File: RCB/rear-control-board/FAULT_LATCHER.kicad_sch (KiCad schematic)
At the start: 8 parts, among them J4 Conn_01x02, J5 Conn_01x02, K2 G5V-2, K3 G5V-2, Q1 BSS84, Q2 2N7002

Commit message: working on layout
Updating traces for RCB and organizing HVB
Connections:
- net bms_switch: now reaches D4.2 (A), J4.1 (Pin_1), K2.1, K2.8, Q1.1 (G)
- net connector: now reaches K2.13, K3.9
- net imd_switch: now reaches D5.1 (K), J5.2 (Pin_2), K3.1, K3.8, Q2.1 (G)
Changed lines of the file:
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@@
+    (effects (font (size 1.27 1.27)) (justify left bottom))
+  )
+  (label "bms_switch" (at 85.09 67.31 90)
     (effects (font (size 1.27 1.27)) (justify left bottom))
   )
@@
     (effects (font (size 1.27 1.27)) (justify right bottom))
   )
+  (label "connector" (at 118.11 46.99 180)
+    (effects (font (size 1.27 1.27)) (justify right bottom))
+  )
+  (label "imd_switch" (at 135.255 67.31 270)
+    (effects (font (size 1.27 1.27)) (justify right bottom))
+  )

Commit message: trace layout complete (need review)
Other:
- note added: "BMS BMS_FAULT_SIG is LOW Clear, HIGH Fault BMS_IND is HIGH when clear, pulled low when fault"
- note added: "IMD IMD_FAULT_SIG is HIGH Clear, LOW Fault IMD_IND is LOW when clear, pulled HIGH when fault"
- note removed: "BMS LOW Clear, HIGH Fault BMS_IND is HIGH when clear, pulled low when fault"
- note removed: "IMD HIGH Clear, LOW Fault IMD_IND is LOW when clear, pulled HIGH when fault"
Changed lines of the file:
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@@
     (effects (font (size 1.27 1.27)) (justify right bottom))
   )
-  (text "IMD\nHIGH Clear, LOW Fault\nIMD_IND is LOW when clear, \npulled HIGH when fault"
+  (text "IMD\nIMD_FAULT_SIG is HIGH Clear, LOW Fault\nIMD_IND is LOW when clear, \npulled HIGH when fault"
     (at 136.525 33.655 0)
     (effects (font (size 1.27 1.27)) (justify left bottom))
   )
-  (text "BMS\nLOW Clear, HIGH Fault\nBMS_IND is HIGH when clear, \npulled low when fault"
+  (text "BMS\nBMS_FAULT_SIG is LOW Clear, HIGH Fault\nBMS_IND is HIGH when clear, \npulled low when fault"
     (at 85.725 33.655 0)
     (effects (font (size 1.27 1.27)) (justify left bottom))

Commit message: Major Review and Part Update
updating footprints, component values, layouts
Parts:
- D4, D5: footprint Diode_THT:D_DO-35_SOD27_P7.62mm_Horizontal -> Diode_SMD:D_SOD-123
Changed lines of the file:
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@@
     (property "Reference" "D5" (id 0) (at 144.78 78.9432 0))
     (property "Value" "1N4148" (id 1) (at 144.78 81.2546 0))
-    (property "Footprint" "Diode_THT:D_DO-35_SOD27_P7.62mm_Horizontal" (id 2) (at 144.78 88.9 0)
+    (property "Footprint" "Diode_SMD:D_SOD-123" (id 2) (at 144.78 88.9 0)
       (effects (font (size 1.27 1.27)) hide)
     )
@@
     (property "Reference" "D4" (id 0) (at 96.52 74.4982 0))
     (property "Value" "1N4148" (id 1) (at 96.52 76.8096 0))
-    (property "Footprint" "Diode_THT:D_DO-35_SOD27_P7.62mm_Horizontal" (id 2) (at 96.52 75.565 0)
+    (property "Footprint" "Diode_SMD:D_SOD-123" (id 2) (at 96.52 75.565 0)
       (effects (font (size 1.27 1.27)) hide)
     )

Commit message: willem review notes
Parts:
- J4, J5: value Conn_01x02 -> JST-B2B-VERT-2PIN
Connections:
- net connector: no longer names the net of K2.13, K3.9
- no-connect marks 0 -> 4
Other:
- note added: "Instead of transistors, use voltage divider and zener diodes"
- note added: "UPERCASE LOCAL NETS ALSO SPREAD OUT SCHEM"
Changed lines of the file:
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@@
   (junction (at 106.68 67.31) (diameter 0) (color 0 0 0 0)
   )
+  (no_connect (at 88.9 49.53))
+  (no_connect (at 88.9 59.69))
+  (no_connect (at 137.16 59.69))
+  (no_connect (at 137.16 49.53))
   (wire (pts (xy 155.575 84.455) (xy 155.575 67.31))
     (stroke (width 0) (type default) (color 0 0 0 0))
@@
     (effects (font (size 1.27 1.27)) (justify right bottom))
   )
+  (text "UPERCASE LOCAL NETS\n\nALSO SPREAD OUT SCHEM" (at 177.165 78.105 0)
+    (effects (font (size 1.27 1.27)) (justify left bottom))
+  )
   (text "IMD\nIMD_FAULT_SIG is HIGH Clear, LOW Fault\nIMD_IND is LOW when clear, \npulled HIGH when fault"
     (at 136.525 33.655 0)
     (effects (font (size 1.27 1.27)) (justify left bottom))
   )
+  (text "Instead of transistors, use voltage divider\nand zener diodes"
+    (at 115.57 107.95 0)
+    (effects (font (size 1.27 1.27)) (justify left bottom))
+  )
   (text "BMS\nBMS_FAULT_SIG is LOW Clear, HIGH Fault\nBMS_IND is HIGH when clear, \npulled low when fault"
     (at 85.725 33.655 0)
@@
   (label "bms_switch" (at 85.09 67.31 90)
     (effects (font (size 1.27 1.27)) (justify left bottom))
-  )
-  (label "Loop_IN" (at 80.645 44.45 0)
-    (effects (font (size 1.27 1.27)) (justify left bottom))
-  )
-  (label "Loop_Out" (at 161.925 46.99 180)
-    (effects (font (size 1.27 1.27)) (justify right bottom))
-  )
-  (label "connector" (at 118.11 46.99 180)
-    (effects (font (size 1.27 1.27)) (justify right bottom))
   )
   (label "imd_switch" (at 135.255 67.31 270)
@@
       (effects (font (size 1.27 1.27)) (justify right))
     )
-    (property "Value" "Conn_01x02" (id 1) (at 120.65 59.69 90)
+    (property "Value" "JST-B2B-VERT-2PIN" (id 1) (at 114.935 59.69 90)
       (effects (font (size 1.27 1.27)) (justify right))
     )
@@
       (effects (font (size 1.27 1.27)) (justify right))
     )
-    (property "Value" "Conn_01x02" (id 1) (at 92.71 85.725 90)
-      (effects (font (size 1.27 1.27)) (justify right))
-    )
+    (property "Value" "JST-B2B-VERT-2PIN" (id 1) (at 92.71 85.725 90)
+      (effects (font (size 1.27 1.27)) (justify right))
+    )

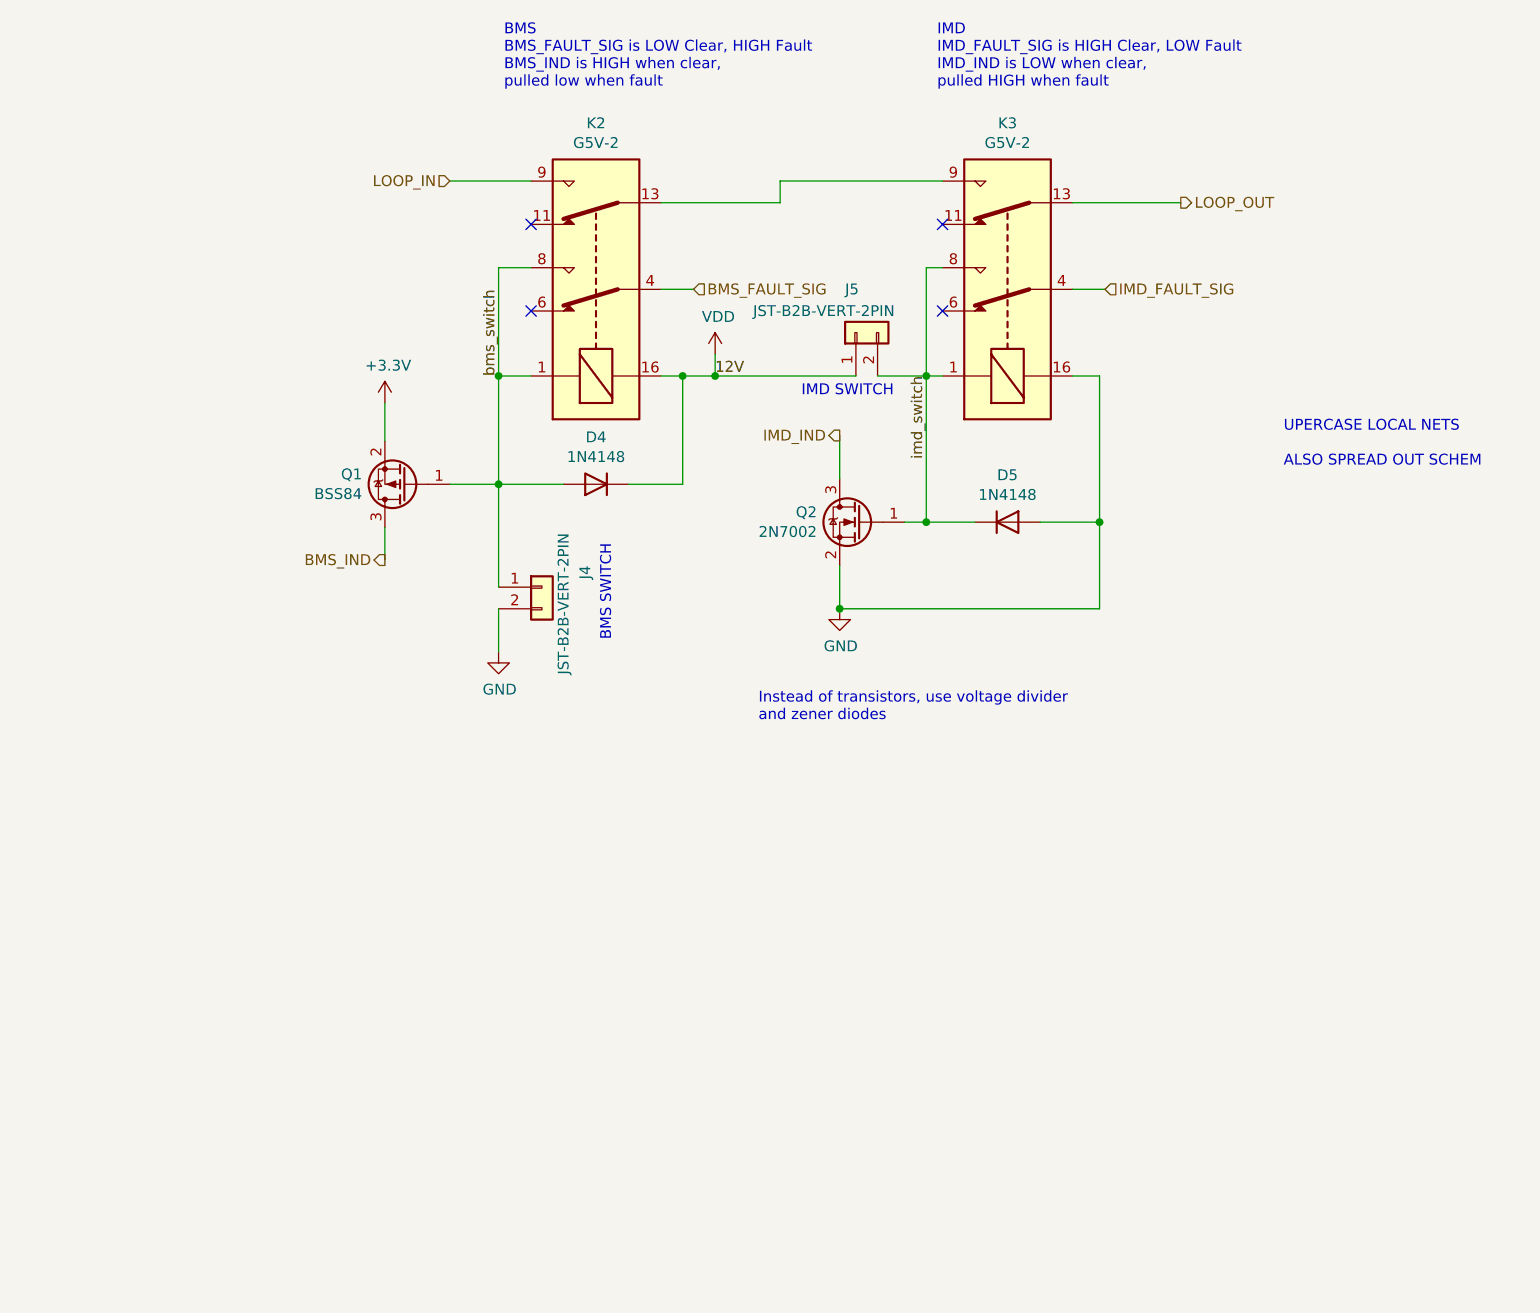
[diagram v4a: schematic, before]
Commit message: updating schem with design notes (major changes)
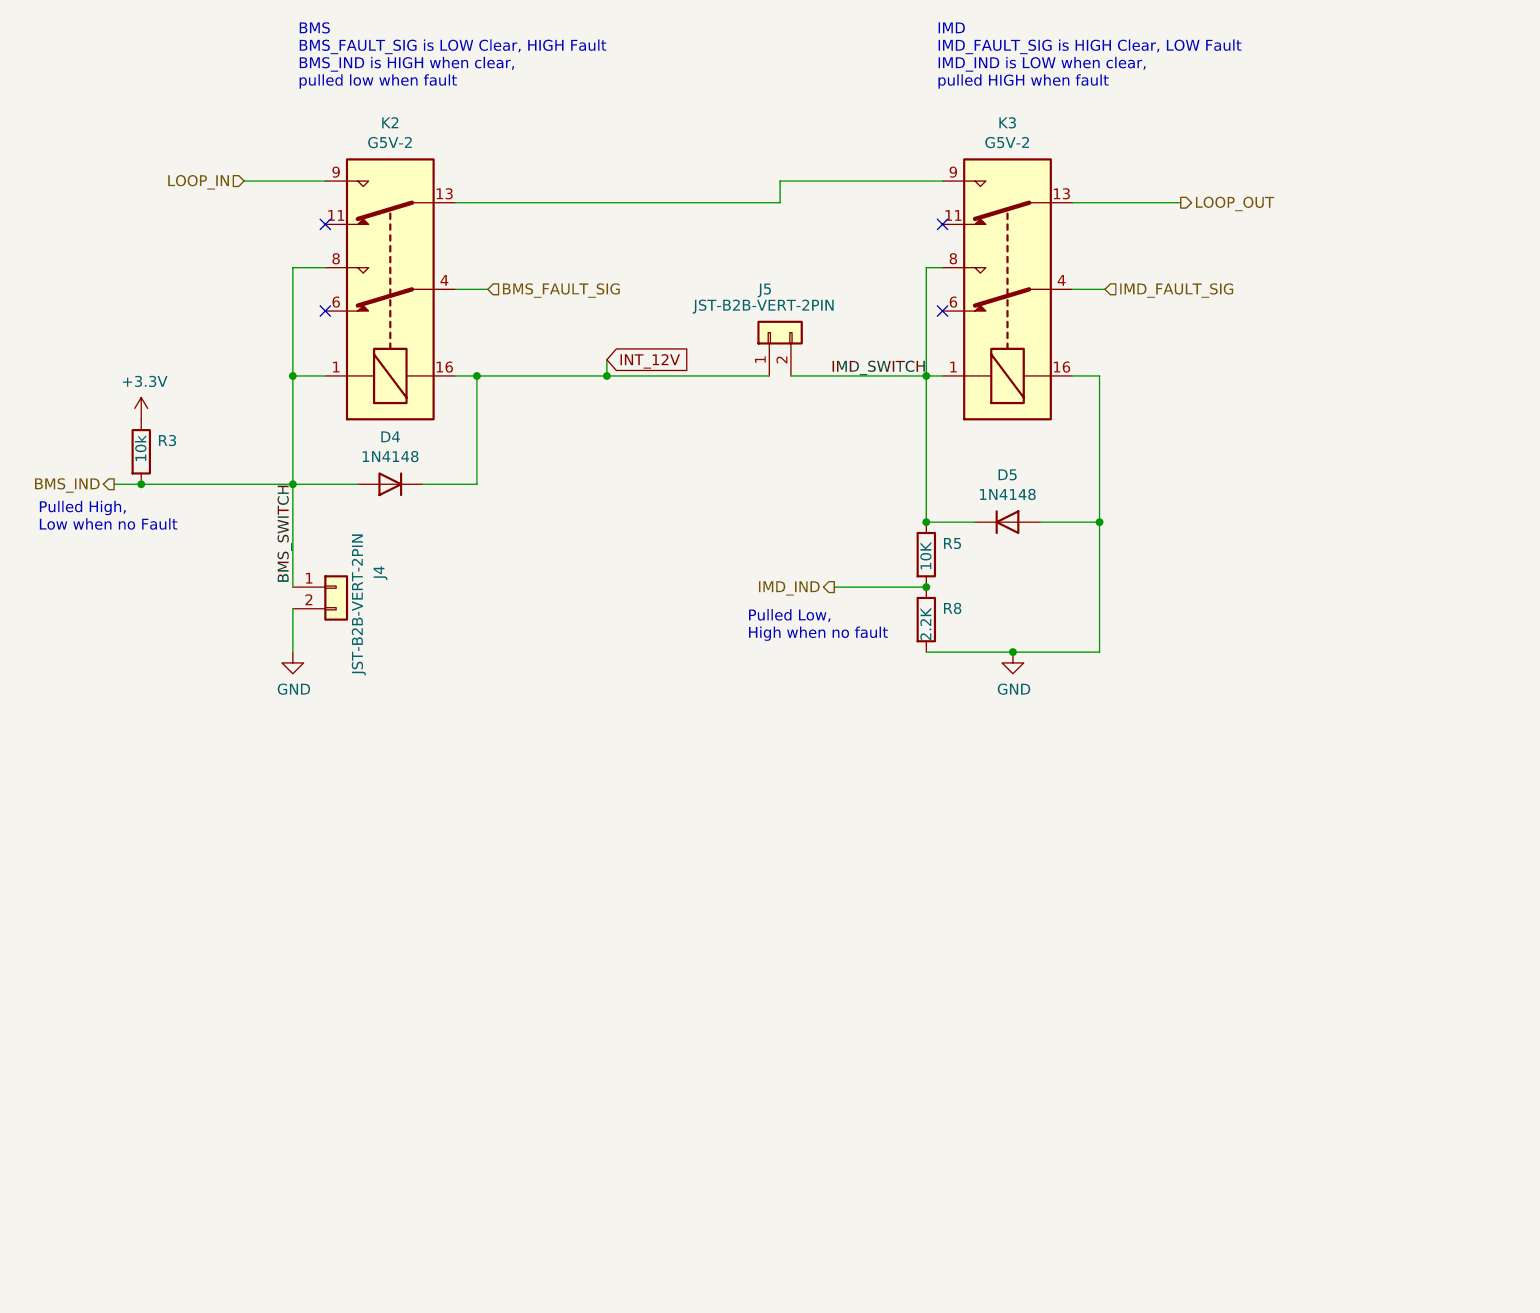
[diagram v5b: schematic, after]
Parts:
- removed Q1: BSS84, Package_TO_SOT_SMD:SOT-23, symbol Transistor_FET:BSS84
- removed Q2: 2N7002, Package_TO_SOT_SMD:SOT-23, symbol Transistor_FET:2N7002
- added R3: 10k, Resistor_SMD:R_0603_1608Metric_Pad0.98x0.95mm_HandSolder, symbol Device:R
- added R5: 10K, Resistor_SMD:R_0603_1608Metric_Pad0.98x0.95mm_HandSolder, symbol Device:R
- added R8: 2.2K, Resistor_SMD:R_0603_1608Metric_Pad0.98x0.95mm_HandSolder, symbol Device:R
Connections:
- net bms_switch is gone; now on net BMS_IND: D4.2 (A), J4.1 (Pin_1), K2.1, K2.8
- net +3V3: now also R3.1
- net BMS_IND: now also R3.2
- net GND: now also R8.2
- net IMD_IND: now also R5.2, R8.1
- net VDD renamed INT_12V
- net imd_switch renamed IMD_SWITCH
- net IMD_SWITCH: now also R5.1
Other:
- note added: "Pulled High, Low when no Fault"
- note added: "Pulled Low, High when no fault"
- note removed: "BMS SWITCH"
- note removed: "IMD SWITCH"
- note removed: "Instead of transistors, use voltage divider and zener diodes"
- note removed: "UPERCASE LOCAL NETS ALSO SPREAD OUT SCHEM"
- moved on the sheet: D4, J4, J5, K2

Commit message: Addded comments
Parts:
- added Q?: B5584, Package_TO_SOT_SMD:SOT-363_SC-70-6, symbol Transistor_BJT:FFB5551
- added R?: 470, symbol Device:R
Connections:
- net +3V3: now also Q?.1 (E1)
- net BMS_IND: now also Q?.6 (C1), R?.1
- net GND: now also R?.2
- new net BMS_SW: Q?.2 (B1)
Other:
- note added: "CHANGED BMS SWITCH"
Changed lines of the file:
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@@
   (junction (at 145.415 99.695) (diameter 0) (color 0 0 0 0)
+  )
+  (junction (at 95.25 135.89) (diameter 0) (color 0 0 0 0)
   )
   (junction (at 135.255 67.31) (diameter 0) (color 0 0 0 0)
@@
   (no_connect (at 137.16 59.69))
   (no_connect (at 137.16 49.53))
+  (wire (pts (xy 63.5 151.765) (xy 66.675 151.765))
+    (stroke (width 0) (type default) (color 0 0 0 0))
+  )
   (wire (pts (xy 155.575 84.455) (xy 155.575 67.31))
     (stroke (width 0) (type default) (color 0 0 0 0))
@@
     (stroke (width 0) (type default) (color 0 0 0 0))
   )
+  (bus (pts (xy 119.38 122.555) (xy 119.38 175.26))
+    (stroke (width 0) (type default) (color 0 0 0 0))
+  )
   (wire (pts (xy 97.79 65.405) (xy 97.79 67.31))
     (stroke (width 0) (type default) (color 0 0 0 0))
@@
     (stroke (width 0) (type default) (color 0 0 0 0))
   )
+  (wire (pts (xy 74.295 156.845) (xy 74.295 166.37))
+    (stroke (width 0) (type default) (color 0 0 0 0))
+  )
+  (wire (pts (xy 74.295 135.89) (xy 95.25 135.89))
+    (stroke (width 0) (type default) (color 0 0 0 0))
+  )
+  (wire (pts (xy 95.25 135.89) (xy 106.68 135.89))
+    (stroke (width 0) (type default) (color 0 0 0 0))
+  )
   (wire (pts (xy 135.255 54.61) (xy 135.255 67.31))
     (stroke (width 0) (type default) (color 0 0 0 0))
@@
     (stroke (width 0) (type default) (color 0 0 0 0))
   )
+  (bus (pts (xy 46.99 122.555) (xy 46.99 175.26))
+    (stroke (width 0) (type default) (color 0 0 0 0))
+  )
   (wire (pts (xy 155.575 84.455) (xy 155.575 99.695))
     (stroke (width 0) (type default) (color 0 0 0 0))
@@
     (stroke (width 0) (type default) (color 0 0 0 0))
   )
+  (bus (pts (xy 46.99 122.555) (xy 119.38 122.555))
+    (stroke (width 0) (type default) (color 0 0 0 0))
+  )
   (wire (pts (xy 135.255 67.31) (xy 137.16 67.31))
     (stroke (width 0) (type default) (color 0 0 0 0))
@@
     (stroke (width 0) (type default) (color 0 0 0 0))
   )
+  (bus (pts (xy 119.38 175.26) (xy 46.99 175.26))
+    (stroke (width 0) (type default) (color 0 0 0 0))
+  )
   (wire (pts (xy 60.96 80.01) (xy 60.96 67.31))
     (stroke (width 0) (type default) (color 0 0 0 0))
@@
   )
   (wire (pts (xy 145.415 99.695) (xy 155.575 99.695))
+    (stroke (width 0) (type default) (color 0 0 0 0))
+  )
+  (wire (pts (xy 74.295 146.685) (xy 74.295 135.89))
     (stroke (width 0) (type default) (color 0 0 0 0))
   )
@@
     (effects (font (size 1.27 1.27)) (justify left bottom))
   )
+  (text "CHANGED BMS SWITCH" (at 31.75 109.855 0)
+    (effects (font (size 1.27 1.27) bold italic) (justify left bottom))
+  )
   (label "BMS_SWITCH" (at 60.96 80.01 270)
     (effects (font (size 1.27 1.27)) (justify right bottom))
@@
   (label "IMD_SWITCH" (at 135.255 67.31 180)
     (effects (font (size 1.27 1.27)) (justify right bottom))
+  )
+  (label "BMS_IND" (at 106.68 135.89 0)
+    (effects (font (size 1.27 1.27) bold italic) (justify left bottom))
   )
   (global_label "INT_12V" (shape input) (at 97.79 65.405 0) (fields_autoplaced)
@@
     (property "Intersheet References" "${INTERSHEET_REFS}" (id 0) (at 107.4923 65.3256 0)
       (effects (font (size 1.27 1.27)) (justify left) hide)
+    )
+  )
+  (global_label "BMS_SW" (shape input) (at 63.5 151.765 180) (fields_autoplaced)
+    (effects (font (size 1.27 1.27) bold italic) (justify right))
+    (property "Intersheet References" "${INTERSHEET_REFS}" (id 0) (at 53.1703 151.638 0)
+      (effects (font (size 1.27 1.27) bold italic) (justify right) hide)
     )
   )
@@
     (pin "1")
   )
+  (symbol (lib_id "power:+3.3V") (at 74.295 166.37 180) (unit 1)
+    (in_bom yes) (on_board yes) (fields_autoplaced)
+    (property "Reference" "#PWR?" (id 0) (at 74.295 162.56 0)
+      (effects (font (size 1.27 1.27)) hide)
+    )
+    (property "Value" "+3.3V" (id 1) (at 74.295 171.45 0))
+    (property "Footprint" "" (id 2) (at 74.295 166.37 0)
+      (effects (font (size 1.27 1.27)) hide)
+    )
+    (property "Datasheet" "" (id 3) (at 74.295 166.37 0)
+      (effects (font (size 1.27 1.27)) hide)
+    )
+    (pin "1")
+  )
+  (symbol (lib_id "Transistor_BJT:FFB5551") (at 71.755 151.765 0) (unit 1)
+    (in_bom yes) (on_board yes) (fields_autoplaced)
+    (property "Reference" "Q?" (id 0) (at 77.47 150.4949 0)
+      (effects (font (size 1.27 1.27)) (justify left))
+    )
+    (property "Value" "B5584" (id 1) (at 77.47 153.0349 0)
+      (effects (font (size 1.27 1.27)) (justify left))
+    )
+    (property "Footprint" "Package_TO_SOT_SMD:SOT-363_SC-70-6" (id 2) (at 76.835 149.225 0)
+      (effects (font (size 1.27 1.27)) hide)
+    )
+    (property "Datasheet" "https://www.onsemi.com/pub/Collateral/FFB5551-D.PDF" (id 3) (at 71.755 151.765 0)
+      (effects (font (size 1.27 1.27)) hide)
+    )
+    (pin "1")
+    (pin "2")
+    (pin "6")
+  )
+  (symbol (lib_id "power:GND") (at 95.25 143.51 0) (unit 1)
+    (in_bom yes) (on_board yes) (fields_autoplaced)
+    (property "Reference" "#PWR?" (id 0) (at 95.25 149.86 0)
+      (effects (font (size 1.27 1.27)) hide)
+    )
+    (property "Value" "GND" (id 1) (at 95.25 148.59 0))
+    (property "Footprint" "" (id 2) (at 95.25 143.51 0)
+      (effects (font (size 1.27 1.27)) hide)
+    )
+    (property "Datasheet" "" (id 3) (at 95.25 143.51 0)
+      (effects (font (size 1.27 1.27)) hide)
+    )
+    (pin "1")
+  )
   (symbol (lib_id "Device:R") (at 135.255 95.885 0) (unit 1)
     (in_bom yes) (on_board yes)
@@
       (effects (font (size 1.27 1.27)) hide)
     )
+    (pin "1")
+    (pin "2")
+  )
+  (symbol (lib_id "Device:R") (at 95.25 139.7 0) (unit 1)
+    (in_bom yes) (on_board yes)
+    (property "Reference" "R?" (id 0) (at 97.79 138.4299 0)
+      (effects (font (size 1.27 1.27)) (justify left))
+    )
+    (property "Value" "470" (id 1) (at 95.25 141.605 90)
+      (effects (font (size 1.27 1.27)) (justify left))
+    )
+    (property "Footprint" "" (id 2) (at 93.472 139.7 90)
+      (effects (font (size 1.27 1.27)) hide)
+    )
+    (property "Datasheet" "~" (id 3) (at 95.25 139.7 0)
+      (effects (font (size 1.27 1.27)) hide)
+    )
